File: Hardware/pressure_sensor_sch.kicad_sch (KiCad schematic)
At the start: 56 parts, among them IC5 ADS131M04IRUKR, J4 1053131104, J5 1053131104, J6 1053131104, J7 1053131104

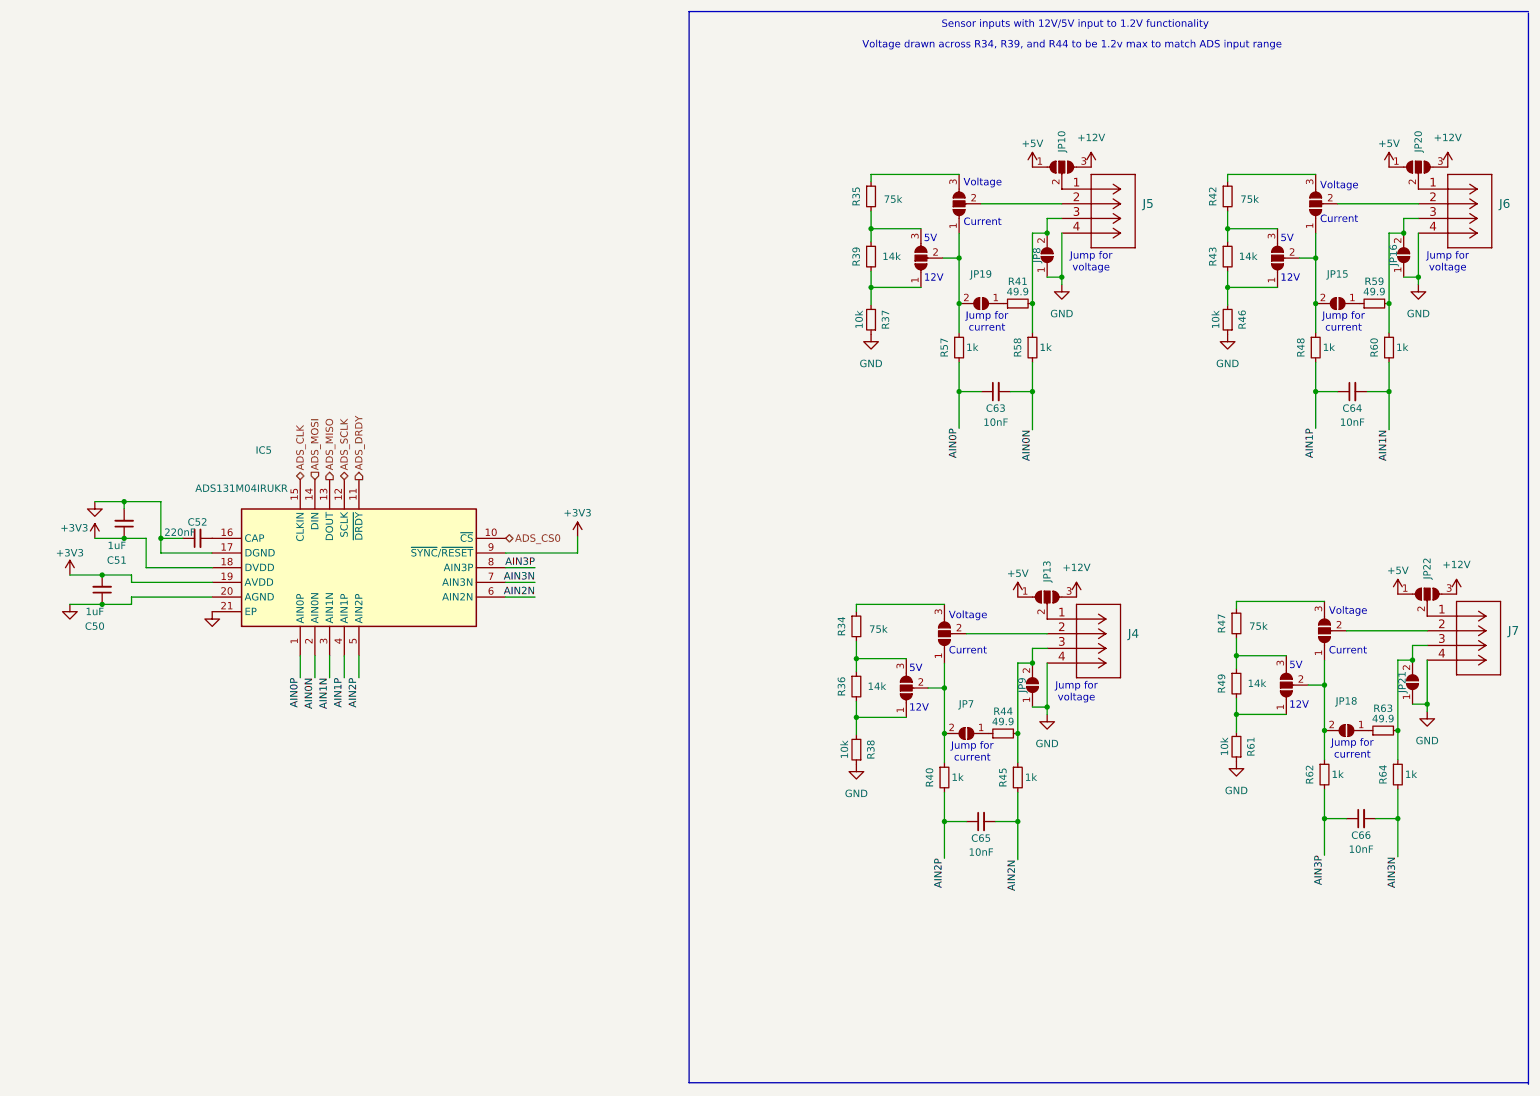
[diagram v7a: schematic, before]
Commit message: updated jumpers and silkscreen labelling
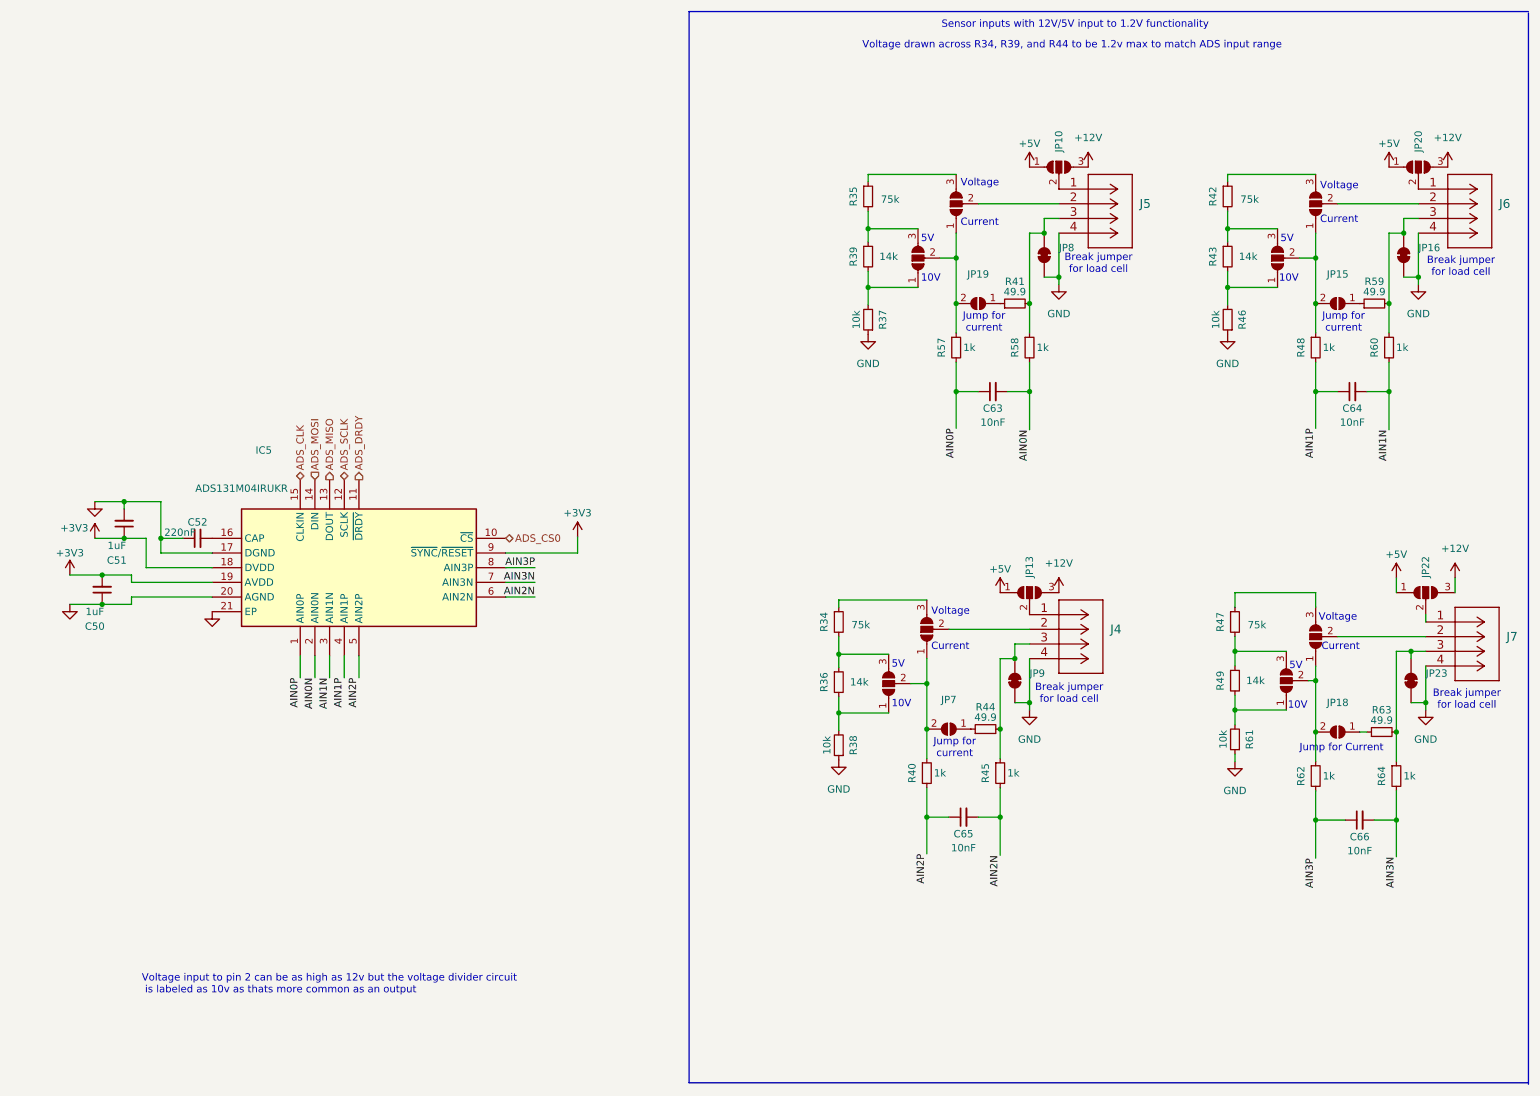
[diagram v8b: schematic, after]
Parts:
- removed JP16, JP21, JP8, JP9: SolderJumper_2_Open, iclr:SmallerSolderJP, symbol Jumper:SolderJumper_2_Open
- added JP16, JP23, JP8, JP9: SolderJumper_2_Bridged, iclr:small_2_pad_jumper_closed, symbol Jumper:SolderJumper_2_Bridged
- IC5: footprint QFN40P300X300X80-21N-D -> iclr:QFN40P300X300X80-21N-D
- JP15, JP18, JP19, JP7: footprint iclr:SmallerSolderJP -> iclr:small_2_pad_jumper_open
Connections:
- net GND: now also JP16.1 (A), JP23.1 (A), JP8.1 (A), JP9.1 (A)
- net at J4.3, R44.2, R45.1: now also JP9.2 (B)
- net at J5.3, R41.2, R58.1: now also JP8.2 (B)
- net at J6.3, R59.2, R60.1: now also JP16.2 (B)
- net at J7.3, R63.2, R64.1: now also JP23.2 (B)
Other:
- note added: "10V"
- note added: "Break jumper for load cell"
- note added: "Jump for Current"
- note added: "Voltage input to pin 2 can be as high as 12v but the voltage divider circuit is labeled as 10v as thats more common as an output"
- note removed: "12V"
- note removed: "Jump for voltage"
- moved on the sheet: C63, C65, J4, J5, J7, JP10, JP13, JP18, JP19, JP7, R34, R35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
